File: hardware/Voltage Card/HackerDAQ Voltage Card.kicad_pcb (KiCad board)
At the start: 2 copper layers, 90 x 90 mm, 88 parts, among them J1 0039301040, J2 0039301040, J3 0039301040, J4 0039301040, J5 0039301040, J6 0039301040, J7 0039301040, J8 0039301040, J9 LD15S33E4GX00LF, U1 AD7770, U2 OPA310xDBV, U3 TLV71333PDBV

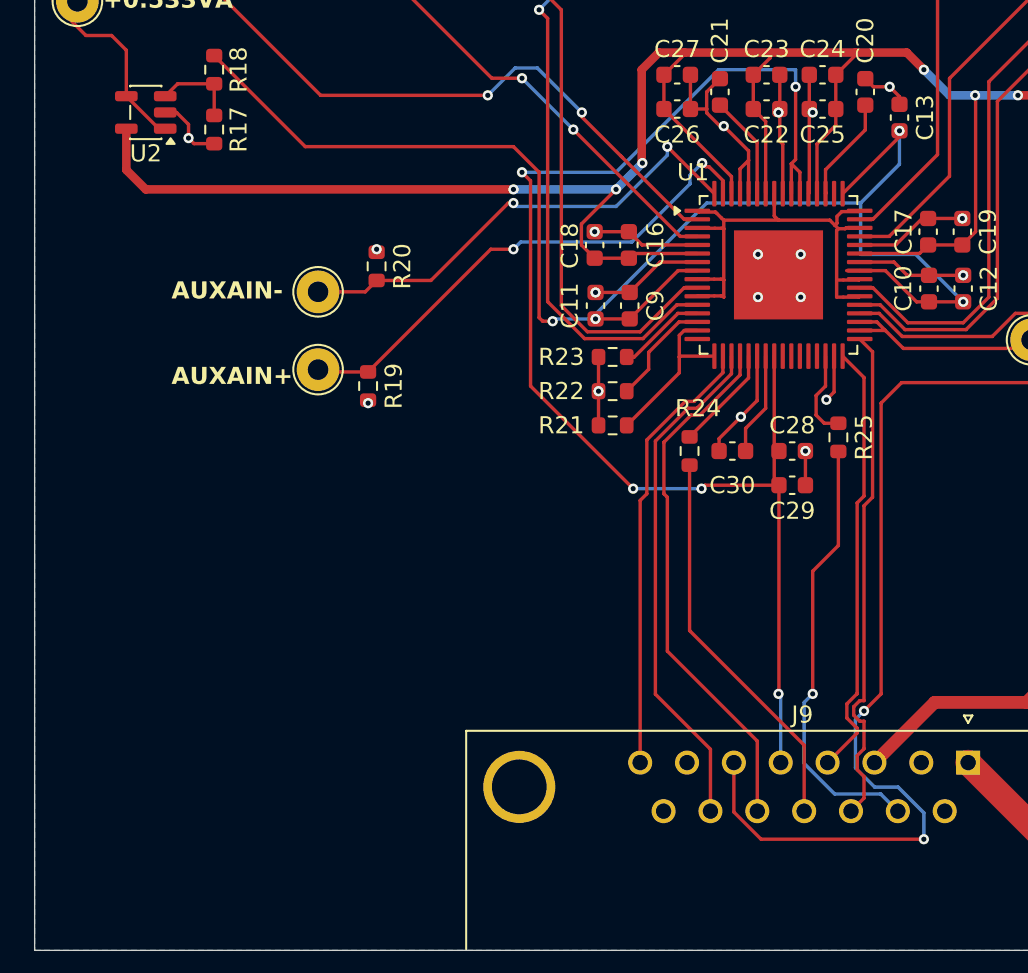
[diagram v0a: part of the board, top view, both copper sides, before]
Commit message: Finish initial voltage card design, add logo
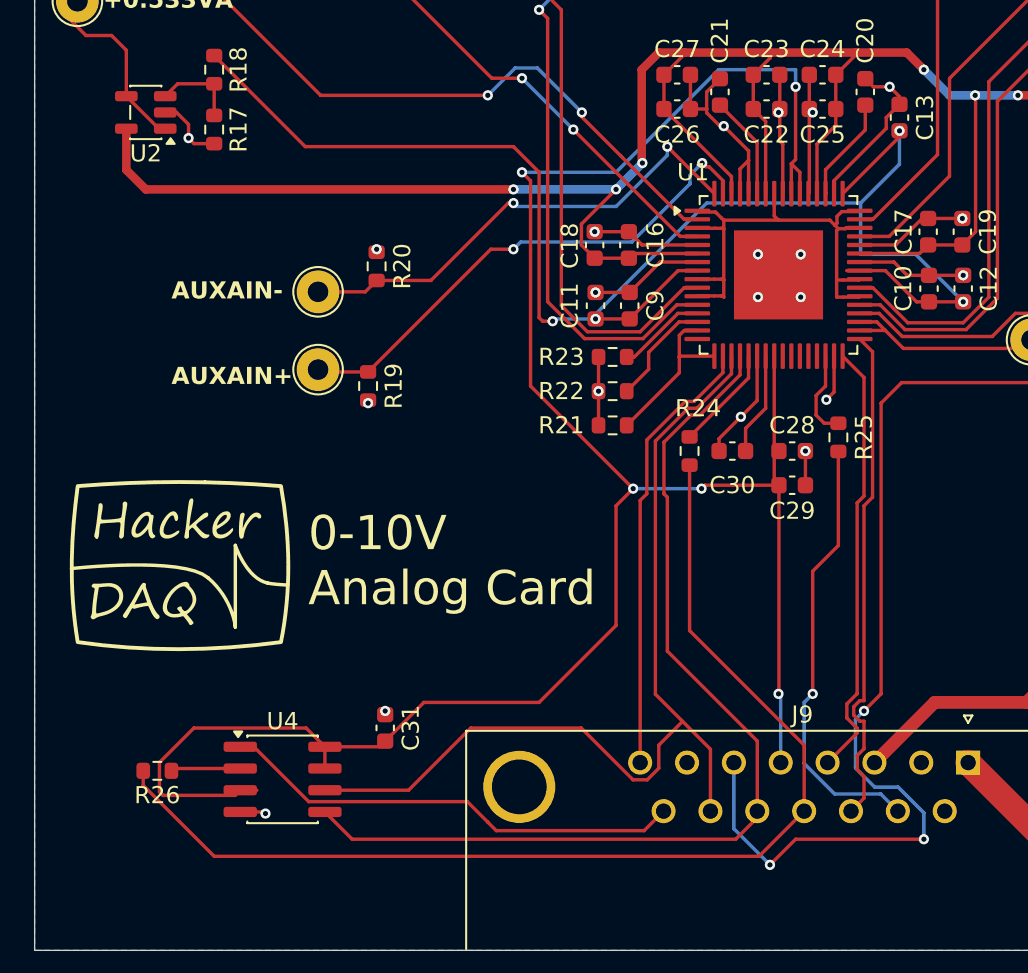
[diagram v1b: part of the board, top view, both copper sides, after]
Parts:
- added C31: 100nF, Capacitor_SMD:C_0603_1608Metric, F.Cu at (70.5, 127.0)
- added LG1: ~, Project Library:HackerDAQ Logo, F.Cu at (58.2, 116.7)
- added R26: 33, Resistor_SMD:R_0603_1608Metric, F.Cu at (57.2, 129.5)
- added U4: M95320-RMN6, Package_SO:SOIC-8_3.9x4.9mm_P1.27mm, F.Cu at (64.5, 130.0)
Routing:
- net +3.3V: track 81.5 -> 129.8 mm
- net /AD7770 ADC/SPI.MISO: track 23.0 -> 65.3 mm
- net /B2B Connector Card Side/CS1: track 0.00 -> 27.3 mm
- net /AD7770 ADC/SPI.MOSI: track 31.0 -> 57.9 mm
- net /AD7770 ADC/SPI.SCLK: track 30.1 -> 56.0 mm
- net GND: track 103.2 -> 111.8 mm, vias 37 -> 39
- net Net-(U4-Q): track 0.00 -> 4.08 mm
- net /AD7770 ADC/~{RESET}: track 69.7 -> 71.5 mm, vias 2 -> 3
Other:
- board text added: "0-10V Analog Card"

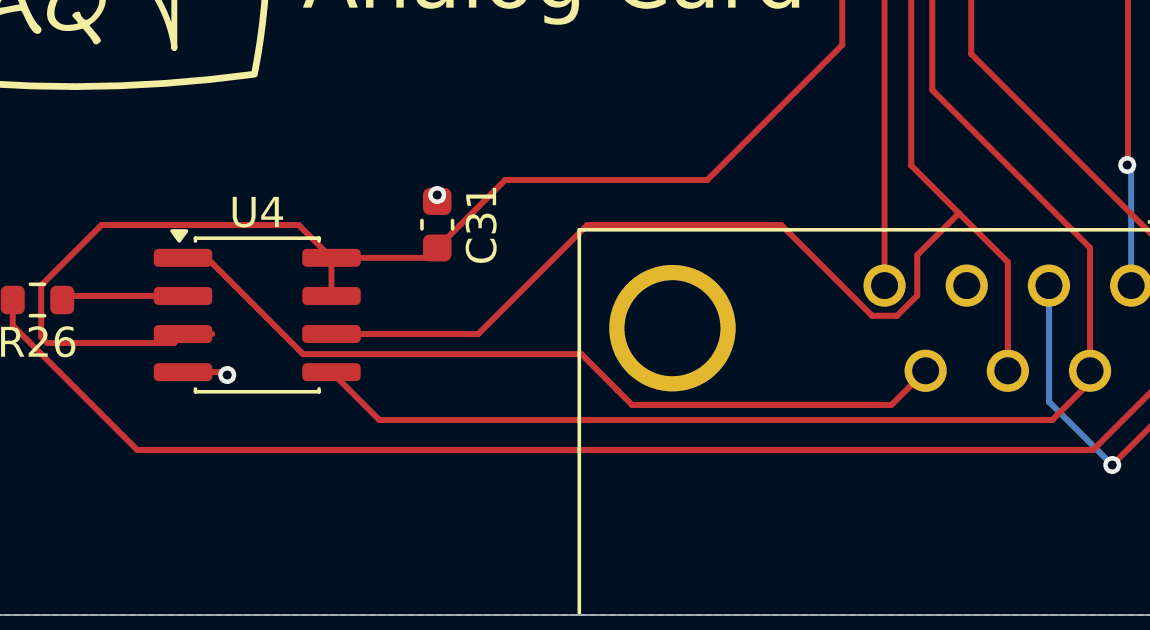
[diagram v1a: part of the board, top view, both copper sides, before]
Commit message: Start on MCU symbol and main unit
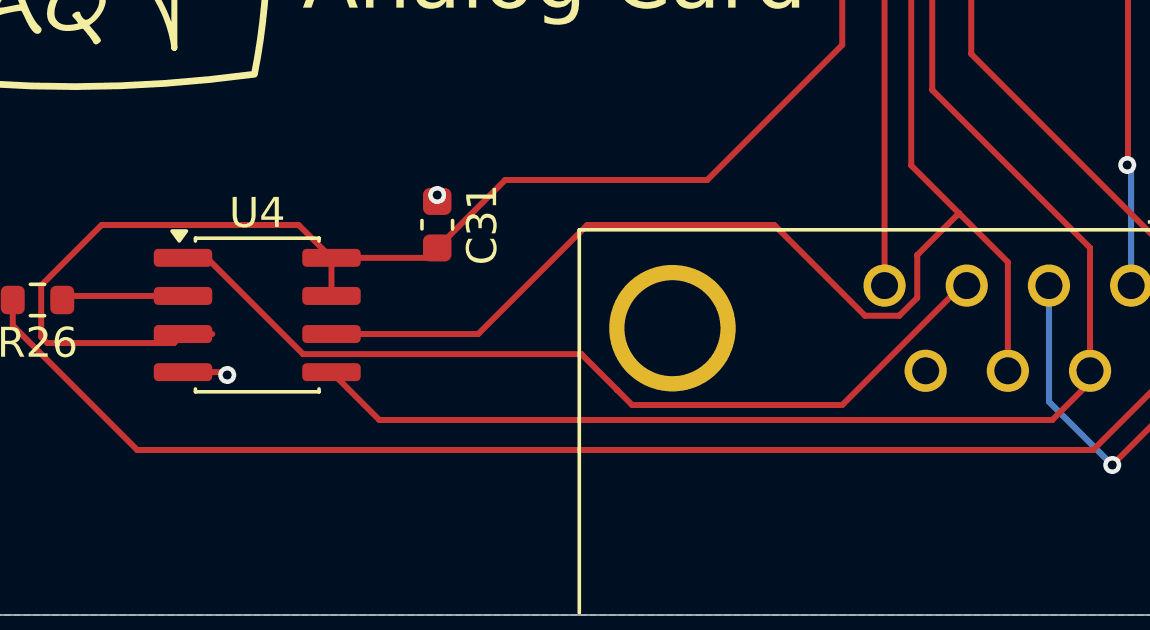
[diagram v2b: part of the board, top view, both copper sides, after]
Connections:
- U4 pad 1: /B2B Connector Card Side/CS1 -> /B2B Connector Card Side/CS2
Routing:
- net /B2B Connector Card Side/CS2: track 0.00 -> 29.8 mm
- net /B2B Connector Card Side/CS1: track 27.3 -> 0.00 mm
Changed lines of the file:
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@@
 			(net 46 "/B2B Connector Card Side/CS2")
 			(pinfunction "7")
-			(pintype "passive+no_connect")
+			(pintype "passive")
 			(solder_mask_margin 0.102)
 		)
@@
 			(net 50 "/B2B Connector Card Side/CS1")
 			(pinfunction "P15")
-			(pintype "passive")
+			(pintype "passive+no_connect")
 			(solder_mask_margin 0.102)
 		)
@@
 			(layers "F.Cu" "F.Mask" "F.Paste")
 			(roundrect_rratio 0.25)
-			(net 50 "/B2B Connector Card Side/CS1")
+			(net 46 "/B2B Connector Card Side/CS2")
 			(pinfunction "~{S}")
 			(pintype "input")
@@
 	)
 	(segment
+		(start 87.980331 129.019669)
+		(end 84 133)
+		(width 0.2)
+		(layer "F.Cu")
+		(net 46)
+	)
+	(segment
+		(start 62.818032 128.095)
+		(end 62.025 128.095)
+		(width 0.2)
+		(layer "F.Cu")
+		(net 46)
+	)
+	(segment
+		(start 66.027032 131.304)
+		(end 62.818032 128.095)
+		(width 0.2)
+		(layer "F.Cu")
+		(net 46)
+	)
+	(segment
+		(start 75.304 131.304)
+		(end 66.027032 131.304)
+		(width 0.2)
+		(layer "F.Cu")
+		(net 46)
+	)
+	(segment
+		(start 84 133)
+		(end 76.996745 133)
+		(width 0.2)
+		(layer "F.Cu")
+		(net 46)
+	)
+	(segment
+		(start 76.996745 133)
+		(end 76.5 132.503255)
+		(width 0.2)
+		(layer "F.Cu")
+		(net 46)
+	)
+	(segment
+		(start 76.5 132.503255)
+		(end 76.5 132.5)
+		(width 0.2)
+		(layer "F.Cu")
+		(net 46)
+	)
+	(segment
+		(start 76.5 132.5)
+		(end 75.304 131.304)
+		(width 0.2)
+		(layer "F.Cu")
+		(net 46)
+	)
+	(segment
+		(start 88.15 129.019669)
+		(end 87.980331 129.019669)
+		(width 0.2)
+		(layer "F.Cu")
+		(net 46)
+	)
+	(segment
 		(start 98.099 113.8339)
 		(end 98.099 124.998)
@@
 	)
 	(segment
-		(start 75.304 131.304)
-		(end 76.5 132.5)
-		(width 0.2)
-		(layer "F.Cu")
-		(net 50)
-	)
-	(segment
-		(start 85.639669 133)
-		(end 86.78 131.859669)
-		(width 0.2)
-		(layer "F.Cu")
-		(net 50)
-	)
-	(segment
-		(start 76.5 132.5)
-		(end 76.5 132.503255)
-		(width 0.2)
-		(layer "F.Cu")
-		(net 50)
-	)
-	(segment
-		(start 66.027032 131.304)
-		(end 75.304 131.304)
-		(width 0.2)
-		(layer "F.Cu")
-		(net 50)
-	)
-	(segment
-		(start 62.818032 128.095)
-		(end 66.027032 131.304)
-		(width 0.2)
-		(layer "F.Cu")
-		(net 50)
-	)
-	(segment
-		(start 76.5 132.503255)
-		(end 76.996745 133)
-		(width 0.2)
-		(layer "F.Cu")
-		(net 50)
-	)
-	(segment
-		(start 62.025 128.095)
-		(end 62.818032 128.095)
-		(width 0.2)
-		(layer "F.Cu")
-		(net 50)
-	)
-	(segment
-		(start 76.996745 133)
-		(end 85.639669 133)
-		(width 0.2)
-		(layer "F.Cu")
-		(net 50)
-	)
-	(segment
 		(start 88.77242 97.77242)
 		(end 88.75 97.75)
@@
 	)
 	(segment
-		(start 87.890808 126.609192)
-		(end 86.5 128)
-		(width 0.2)
-		(layer "F.Cu")
-		(net 62)
-	)
-	(segment
 		(start 88.7339 108.299)
 		(end 88.219836 108.299)
@@
 	)
 	(segment
-		(start 85.826285 130.024669)
-		(end 84.993715 130.024669)
+		(start 86.3 110.218836)
+		(end 86.3 125.018384)
 		(width 0.2)
 		(layer "F.Cu")
@@
 	)
 	(segment
-		(start 84.993715 130.024669)
-		(end 81.969046 127)
+		(start 90.75 105.25)
+		(end 90.75 106.2829)
 		(width 0.2)
 		(layer "F.Cu")
@@
 	)
 	(segment
-		(start 86.3 110.218836)
-		(end 86.3 125.018384)
+		(start 75.5 127)
+		(end 71.865 130.635)
 		(width 0.2)
 		(layer "F.Cu")
@@
 	)
 	(segment
-		(start 90.75 105.25)
-		(end 90.75 106.2829)
+		(start 84.759192 130.024669)
+		(end 81.734523 127)
 		(width 0.2)
 		(layer "F.Cu")
@@
 	)
 	(segment
-		(start 75.5 127)
-		(end 71.865 130.635)
+		(start 81.734523 127)
+		(end 75.5 127)
 		(width 0.2)
 		(layer "F.Cu")
@@
 	)
 	(segment
-		(start 86.5 129.350954)
-		(end 85.826285 130.024669)
+		(start 86.5 129.425477)
+		(end 85.900808 130.024669)
 		(width 0.2)
 		(layer "F.Cu")
@@
 	)
 	(segment
-		(start 81.969046 127)
-		(end 75.5 127)
+		(start 71.865 130.635)
+		(end 66.975 130.635)
 		(width 0.2)
 		(layer "F.Cu")
@@
 	)
 	(segment
-		(start 71.865 130.635)
-		(end 66.975 130.635)
+		(start 89.52 128.238384)
+		(end 89.52 131.859669)
 		(width 0.2)
 		(layer "F.Cu")
@@
 	)
 	(segment
-		(start 89.52 128.238384)
-		(end 89.52 131.859669)
+		(start 87.890808 126.609192)
+		(end 86.5 128)
 		(width 0.2)
 		(layer "F.Cu")
@@
 	)
 	(segment
-		(start 86.5 128)
-		(end 86.5 129.350954)
+		(start 85.900808 130.024669)
+		(end 84.759192 130.024669)
 		(width 0.2)
 		(layer "F.Cu")
@@
 		(width 0.2)
 		(layer "F.Cu")
+		(net 62)
+	)
+	(segment
+		(start 86.5 128)
+		(end 86.5 129.425477)
+		(width 0.2)
+		(layer "F.Cu")

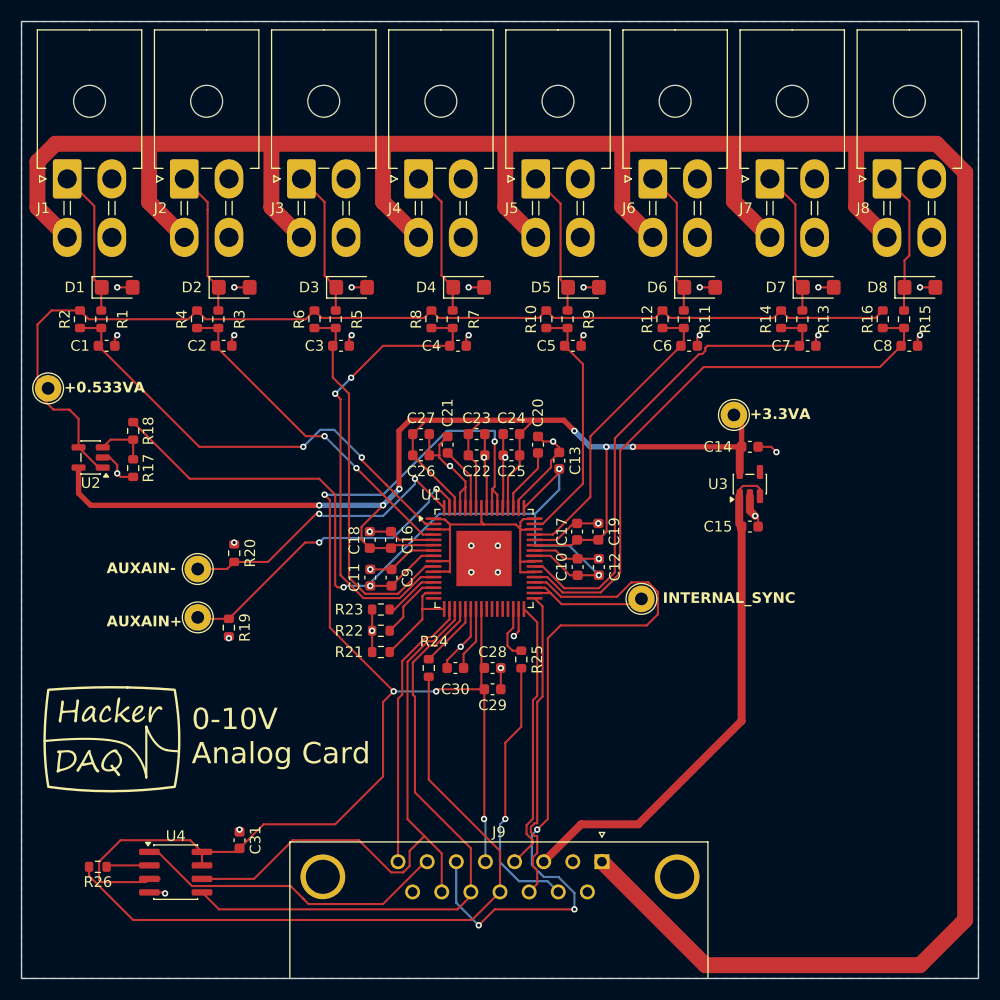
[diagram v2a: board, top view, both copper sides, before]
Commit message: Route more of main unit, start on KiBot CI job
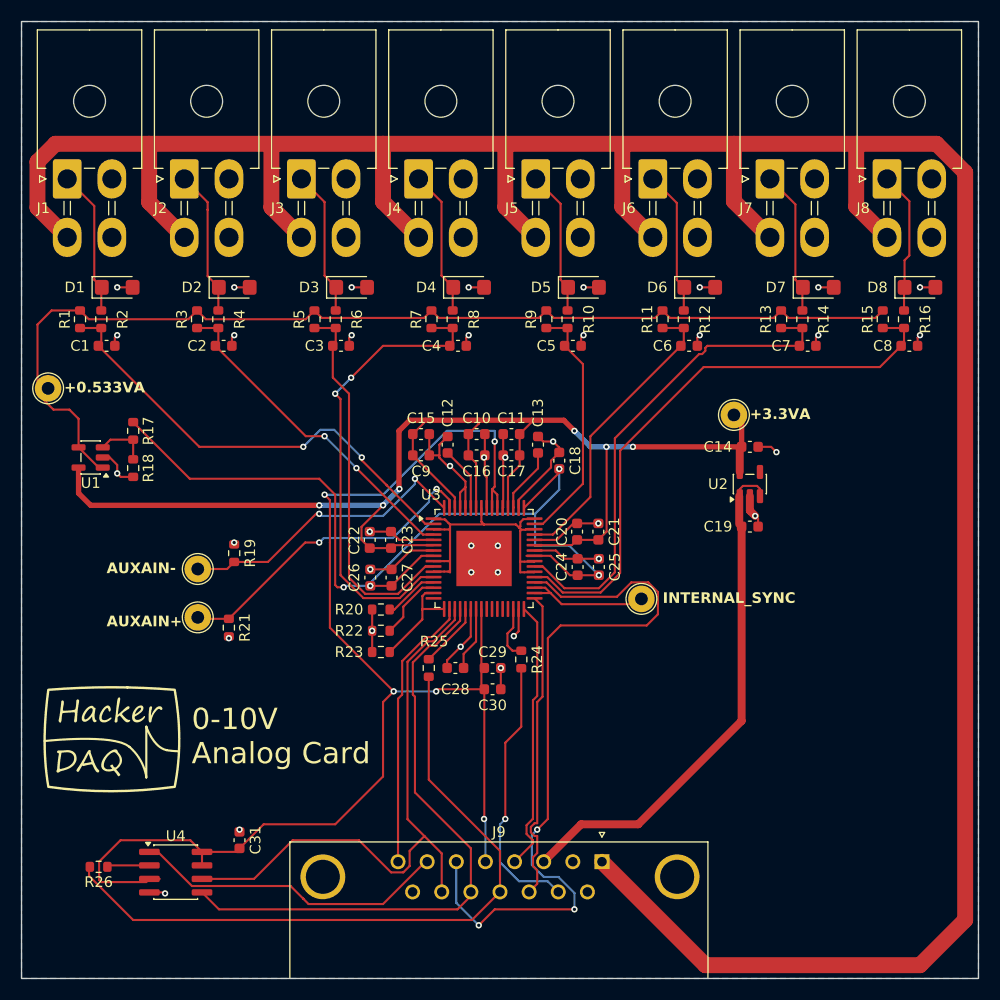
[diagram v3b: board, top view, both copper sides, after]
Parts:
- moved R26 0.08 mm to (57.2, 129.5)
- renumbered C23 to C10, C24 to C11, C21 to C12, C20 to C13, C27 to C15, C22 to C16, C25 to C17, C13 to C18, C15 to C19, C17 to C20, C19 to C21, C18 to C22, C16 to C23, C10 to C24, C12 to C25, C11 to C26, C9 to C27, C30 to C28, C28 to C29, C29 to C30, C26 to C9, NT5 to NT2, NT2 to NT3, NT6 to NT4, NT3 to NT5, NT7 to NT6, NT4 to NT7, R2 to R1, R9 to R10, R12 to R11, R11 to R12, R14 to R13, R13 to R14, R16 to R15, R15 to R16, R18 to R17, R17 to R18, R20 to R19, R1 to R2, R23 to R20, R19 to R21, R21 to R23, R25 to R24, R24 to R25, R4 to R3, R3 to R4, R6 to R5, R5 to R6, R8 to R7, R7 to R8, R10 to R9, TP4 to TP1, TP5 to TP2, TP1 to TP3, TP3 to TP4, TP2 to TP5, U2 to U1, U3 to U2, U1 to U3

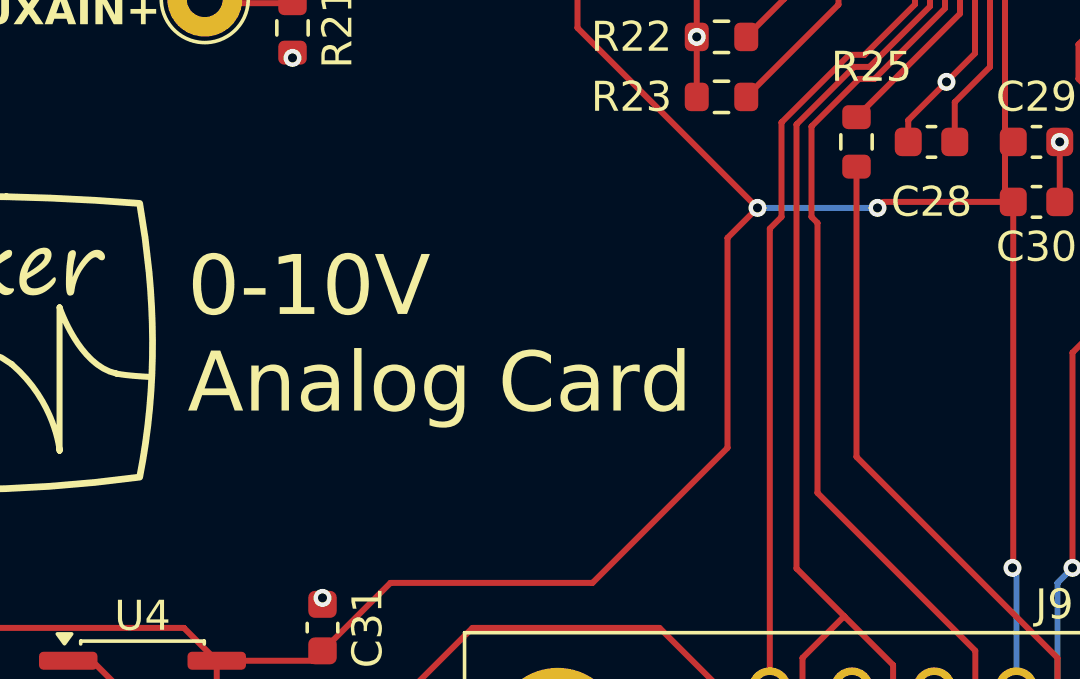
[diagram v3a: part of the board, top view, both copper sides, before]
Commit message: Add Main Unit to CI build as well
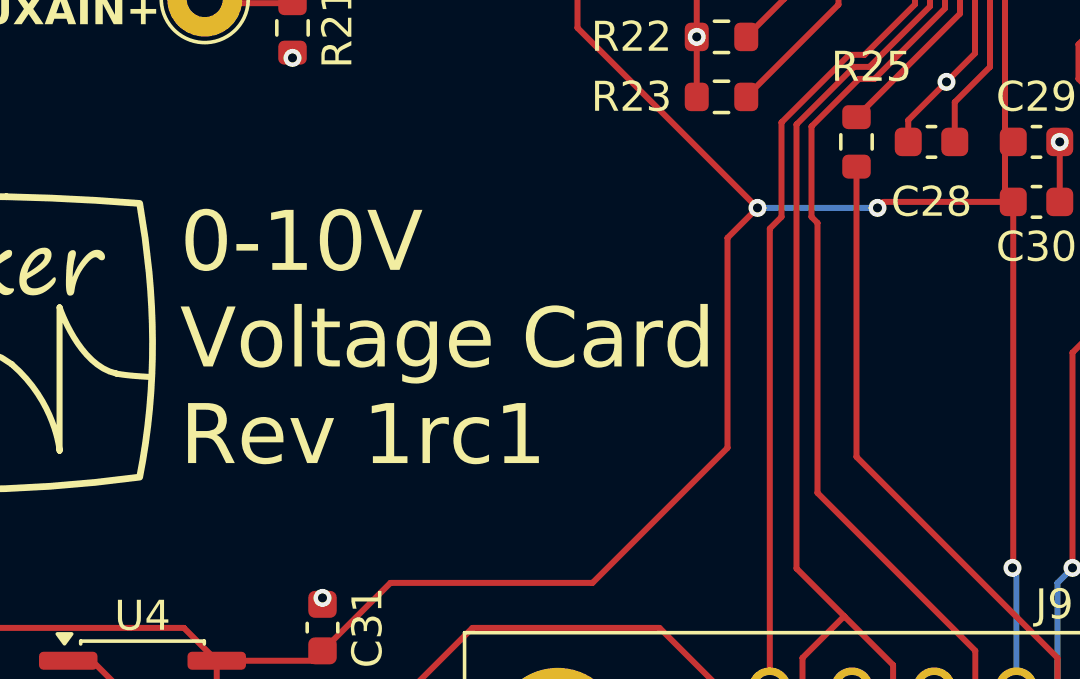
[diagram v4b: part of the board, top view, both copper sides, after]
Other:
- board text added: "0-10V Voltage Card Rev 1rc1"
- board text removed: "0-10V Analog Card"
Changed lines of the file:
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@@
 		)
 	)
+	(property "date" "2026-05-02")
+	(property "version" "2a2f42f")
 	(net 0 "")
 	(net 1 "/AD7770 ADC/AIN+0")
@@
 		)
 	)
-	(gr_text "0-10V\nAnalog Card"
-		(at 66 120 0)
+	(gr_text "0-10V\nVoltage Card\nRev 1rc1"
+		(at 65.75 121.75 0)
 		(layer "F.SilkS")
 		(effects
